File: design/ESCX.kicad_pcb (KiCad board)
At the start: 4 copper layers, 100 x 100 mm, 130 parts, among them J1 SWD, J10 Screw_Terminal_01x03, J11 Screw_Terminal_01x02, J2 Conn_Coaxial, J8 HALL_ENC, J9 USB_C_Receptacle_USB2.0_16P, Q1 IRF7854, Q2 IRF7854, Q3 IRF7854, Q4 IRF7854, Q5 IRF7854, Q6 IRF7854, SW1 SENSOR_VOLTAGE, U1 STM32F40X_LQFP64, U2 LM3671, U3 DRV8301, U4 nRF24L01P, U5 AD8418, U6 AD8418, U7 AD8418, X1 8MHz, X2 16MHz

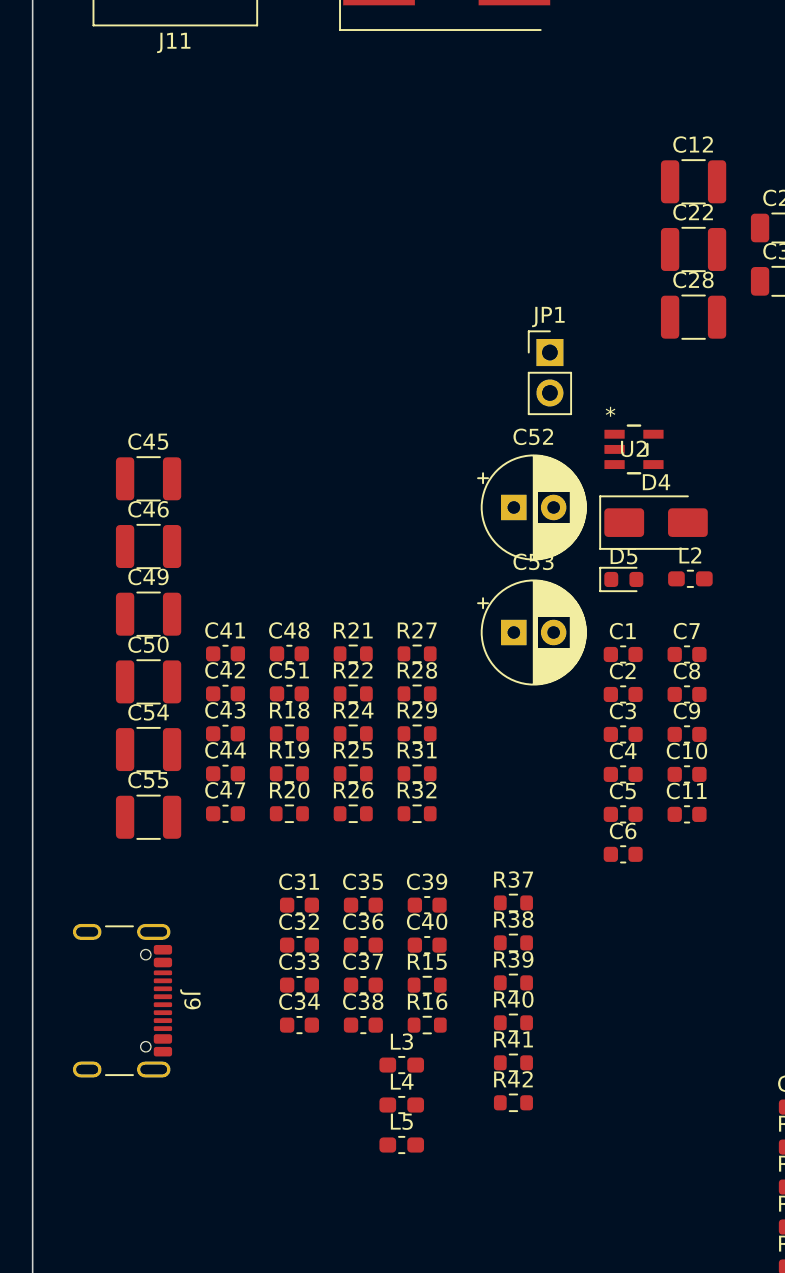
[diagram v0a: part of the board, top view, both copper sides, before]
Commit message: Ubico componentes de USB
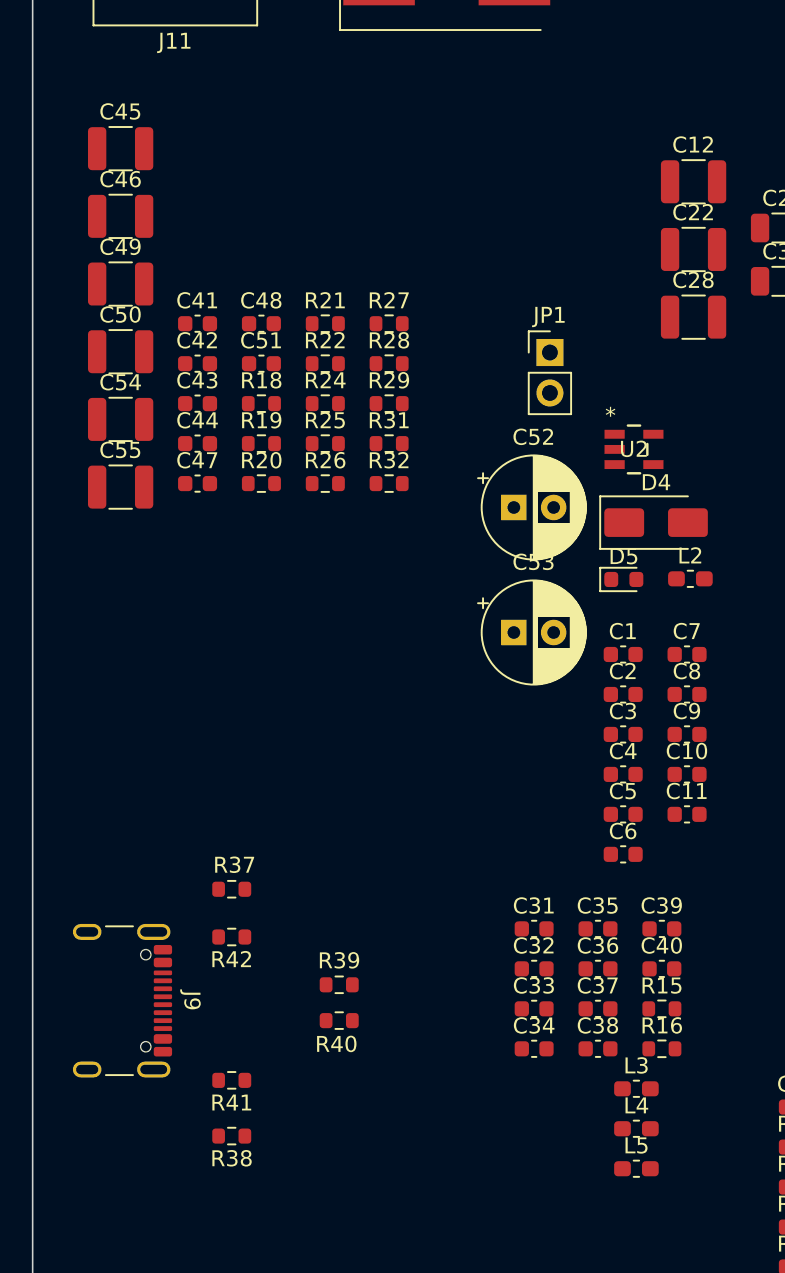
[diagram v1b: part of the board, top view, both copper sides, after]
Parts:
- moved R38 21.4 mm to (111.5, 115.5), turned to 180 degrees
- moved C41 20.8 mm to (109.4, 64.5)
- moved C42 20.8 mm to (109.4, 67.0)
- moved C44 20.8 mm to (109.4, 72.0)
- moved C45 20.8 mm to (104.5, 53.5)
- moved C46 20.8 mm to (104.5, 57.8)
- moved C47 20.8 mm to (109.4, 74.5)
- moved C48 20.8 mm to (113.4, 64.5)
- moved C49 20.8 mm to (104.5, 62.0)
- moved C50 20.8 mm to (104.5, 66.2)
- moved C51 20.8 mm to (113.4, 67.0)
- moved C54 20.8 mm to (104.5, 70.5)
- moved C55 20.8 mm to (104.5, 74.8)
- moved R19 20.8 mm to (113.4, 72.0)
- moved R20 20.8 mm to (113.4, 74.5)
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
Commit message: inicio ruteo de MCU y USB
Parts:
- moved X1 79.9 mm to (150.5, 119.2), turned to 180 degrees
- moved C33 30.2 mm to (109.8, 85.5)
- moved C37 30.2 mm to (113.8, 85.5)
- moved L4 30.2 mm to (116.2, 93.0)
- moved C31 30.2 mm to (109.8, 80.5)
- moved C32 30.2 mm to (109.8, 83.0)
- moved C34 30.2 mm to (109.8, 88.0)
- moved C35 30.2 mm to (113.8, 80.5)
- moved C36 30.2 mm to (113.8, 83.0)
- moved C38 30.2 mm to (113.8, 88.0)
- moved L3 30.2 mm to (116.2, 90.5)
- moved L5 30.2 mm to (116.2, 95.6)
- moved R15 30.2 mm to (117.8, 85.5)
- moved C39 30.2 mm to (117.8, 80.5)
- moved C40 30.2 mm to (117.8, 83.0)
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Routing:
- net /MCU/NRST: track 0.00 -> 25.1 mm, vias 0 -> 2
- net /MCU/SWCLK: track 0.00 -> 19.0 mm, vias 0 -> 2
- net Net-(J9-D+-PadA6): track 0.00 -> 18.3 mm
- net /MCU/USB_DM: track 0.00 -> 18.2 mm
- net Net-(U1-PH1-OSC_OUT): track 0.00 -> 17.1 mm
- net /MCU/USB_DP: track 0.00 -> 16.6 mm
- net /MCU/SWDIO: track 0.00 -> 16.3 mm
- net Net-(J9-VBUS-PadA4): track 0.00 -> 14.6 mm
- net Net-(J9-D--PadA7): track 0.00 -> 10.3 mm
- net Net-(U1-PH0-OSC_IN): track 0.00 -> 9.59 mm
- net Net-(J9-CC2): track 0.00 -> 9.51 mm
- net Net-(J9-CC1): track 0.00 -> 5.95 mm

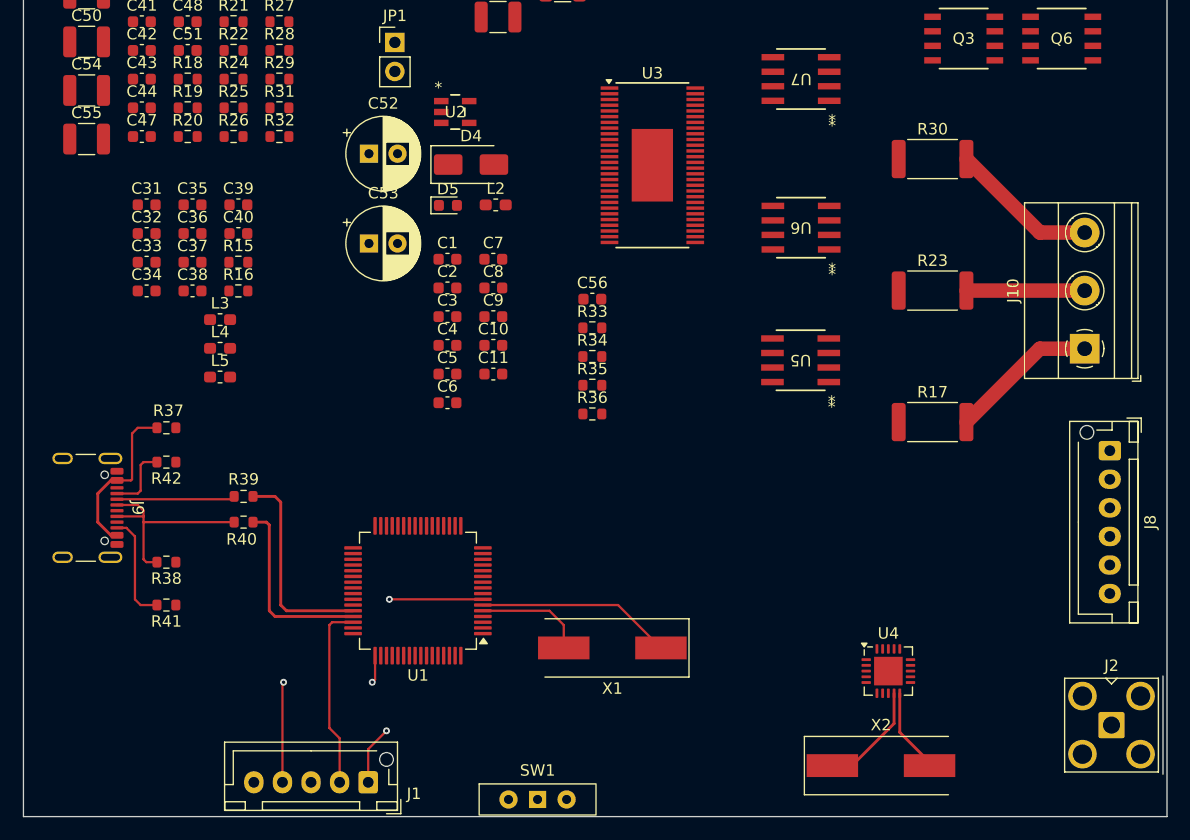
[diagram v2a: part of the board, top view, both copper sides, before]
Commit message: Continue rooteo del MCU y modulo BT
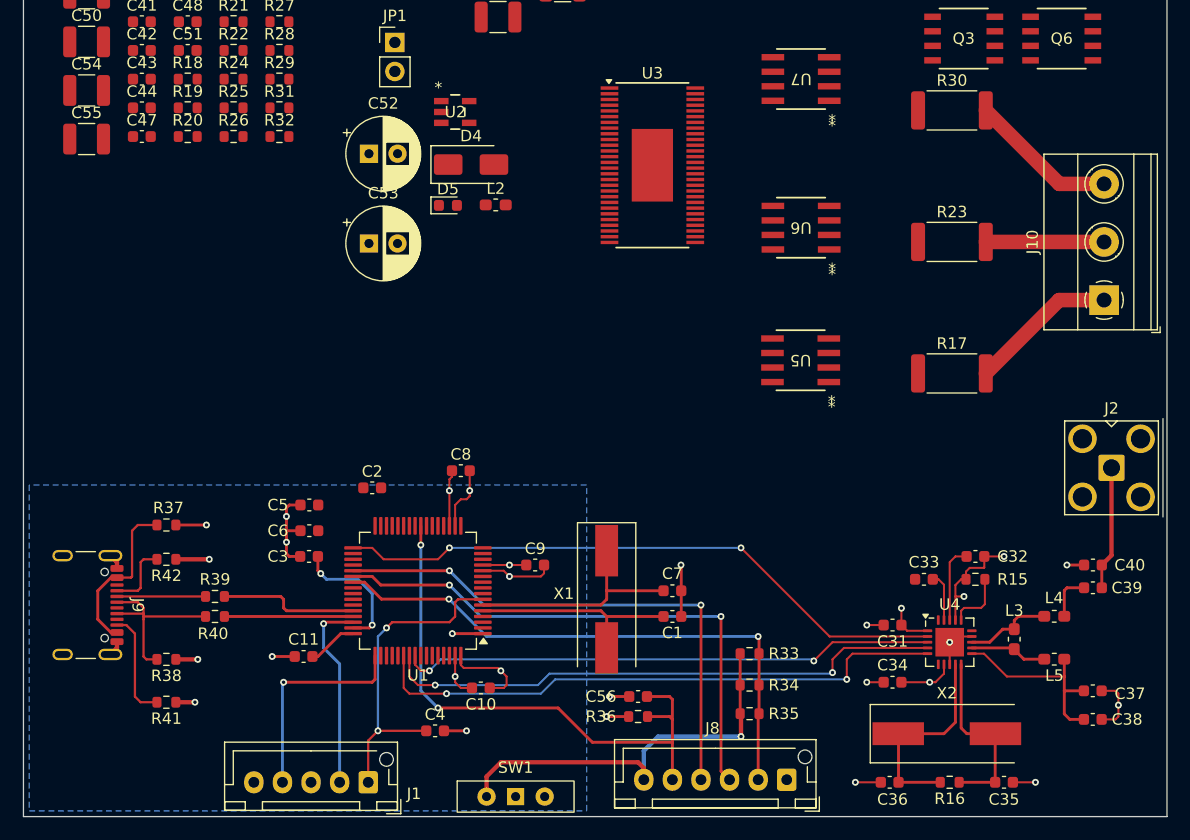
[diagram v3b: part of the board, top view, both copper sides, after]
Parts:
- moved C37 87.2 mm to (192.5, 123.0)
- moved C38 87.2 mm to (192.5, 125.5)
- moved C35 87.1 mm to (184.8, 131.0), turned to 180 degrees
- moved C39 81.9 mm to (192.5, 114.0), turned to 180 degrees
- moved C40 80.2 mm to (192.5, 112.0), turned to 180 degrees
- moved C32 77.8 mm to (182.2, 111.2)
- moved C36 77.6 mm to (174.8, 131.0)
- moved L5 77.0 mm to (189.1, 120.2), turned to 180 degrees
- moved L4 76.6 mm to (189.1, 116.5), turned to 180 degrees
- moved R16 75.6 mm to (180.0, 131.0), turned to 180 degrees
- moved C31 74.9 mm to (175.0, 117.2), turned to 180 degrees
- moved L3 74.9 mm to (185.6, 118.5), turned to -90 degrees
- moved C34 73.7 mm to (175.0, 122.2), turned to 180 degrees
- moved C33 73.4 mm to (177.8, 113.2)
- moved R15 70.2 mm to (182.2, 113.2)
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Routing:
- net GND1: track 0.00 -> 69.3 mm, vias 0 -> 20
- net /MCU/PB12: track 0.00 -> 54.3 mm, vias 0 -> 2
- net /MCU/PD2: track 0.00 -> 51.3 mm, vias 0 -> 2
- net /MCU/HALL_3: track 0.00 -> 50.0 mm, vias 0 -> 2
- net /MCU/TEMP_MOTOR: track 0.00 -> 49.9 mm, vias 0 -> 2
- net /MCU/PB3: track 0.00 -> 49.5 mm, vias 0 -> 2
- net /MCU/HALL_2: track 0.00 -> 48.2 mm, vias 0 -> 2
- net /MCU/PB4: track 0.00 -> 47.0 mm, vias 0 -> 2
- net /MCU/HALL_1: track 0.00 -> 46.9 mm, vias 0 -> 2
- net +3.3V: track 0.00 -> 42.8 mm, vias 0 -> 8
- net Net-(J8-Pin_6): track 0.00 -> 36.1 mm, vias 0 -> 1
- net Net-(U4-VDD_PA): track 0.00 -> 17.3 mm
- net Net-(U1-VCAP2): track 0.00 -> 11.4 mm, vias 0 -> 2
- net Net-(J2-In): track 0.00 -> 10.8 mm
- net Net-(U1-PH0-OSC_IN): track 9.59 -> 18.8 mm
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- added copper zone on In2.Cu, net +3.3V
- added copper zone on B.Cu, net +5V
- added copper zone on In1.Cu, net GND1

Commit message: Continuacion de Rooteo
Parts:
- moved C16 80.4 mm to (77.4, 73.0)
- moved C19 80.4 mm to (77.4, 80.6)
- moved R10 80.4 mm to (89.4, 73.0)
- moved R11 80.4 mm to (89.4, 75.5)
- moved R13 80.4 mm to (89.4, 80.6)
- moved C13 80.4 mm to (77.4, 70.5)
- moved C18 80.4 mm to (77.4, 78.0)
- moved C20 80.4 mm to (77.4, 83.1)
- moved C23 80.4 mm to (81.4, 70.5)
- moved C24 80.4 mm to (81.4, 73.0)
- moved C27 80.4 mm to (81.4, 80.6)
- moved C29 80.4 mm to (81.4, 83.1)
- moved R12 80.4 mm to (89.4, 78.0)
- moved R14 80.4 mm to (89.4, 83.1)
- moved R9 80.4 mm to (89.4, 70.5)
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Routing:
- net +5V: track 2.67 -> 27.8 mm, vias 1 -> 2
- net /DRV8301/FAULT: track 0.00 -> 24.8 mm, vias 0 -> 2
- net /DRV8301/EN_GATE: track 0.00 -> 22.9 mm, vias 0 -> 2
- net /DRV8301/SDI: track 0.00 -> 21.5 mm, vias 0 -> 2
- net /DRV8301/SDO: track 0.00 -> 19.2 mm, vias 0 -> 2
- net /DRV8301/SCLK: track 0.00 -> 17.7 mm, vias 0 -> 2
- net GND1: track 69.3 -> 79.8 mm, vias 20 -> 25
- net Net-(U3-SS_TR): track 0.00 -> 10.2 mm
- net Net-(D4-K): track 0.00 -> 9.41 mm
- net SUPPLY: track 0.00 -> 7.69 mm
- net Net-(U3-BST_BK): track 0.00 -> 7.00 mm
- net +3.3V: track 42.8 -> 48.4 mm, vias 8 -> 11
- net /MCU/PB12: track 54.3 -> 58.1 mm
- net Net-(U1-VCAP1): track 0.00 -> 3.34 mm

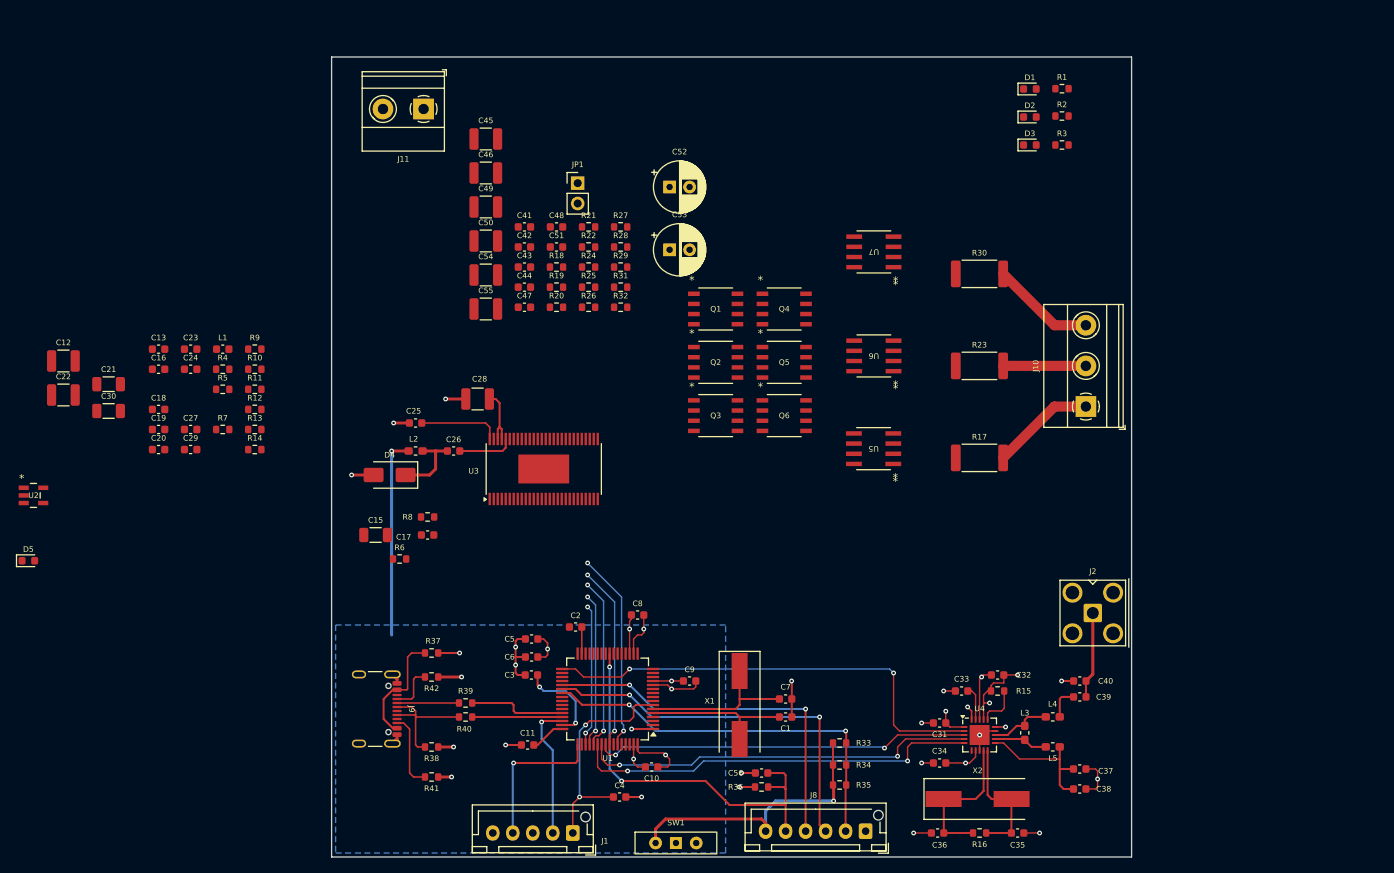
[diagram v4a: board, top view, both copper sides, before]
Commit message: Ruteo del driver y ubicacion de MOSFETs
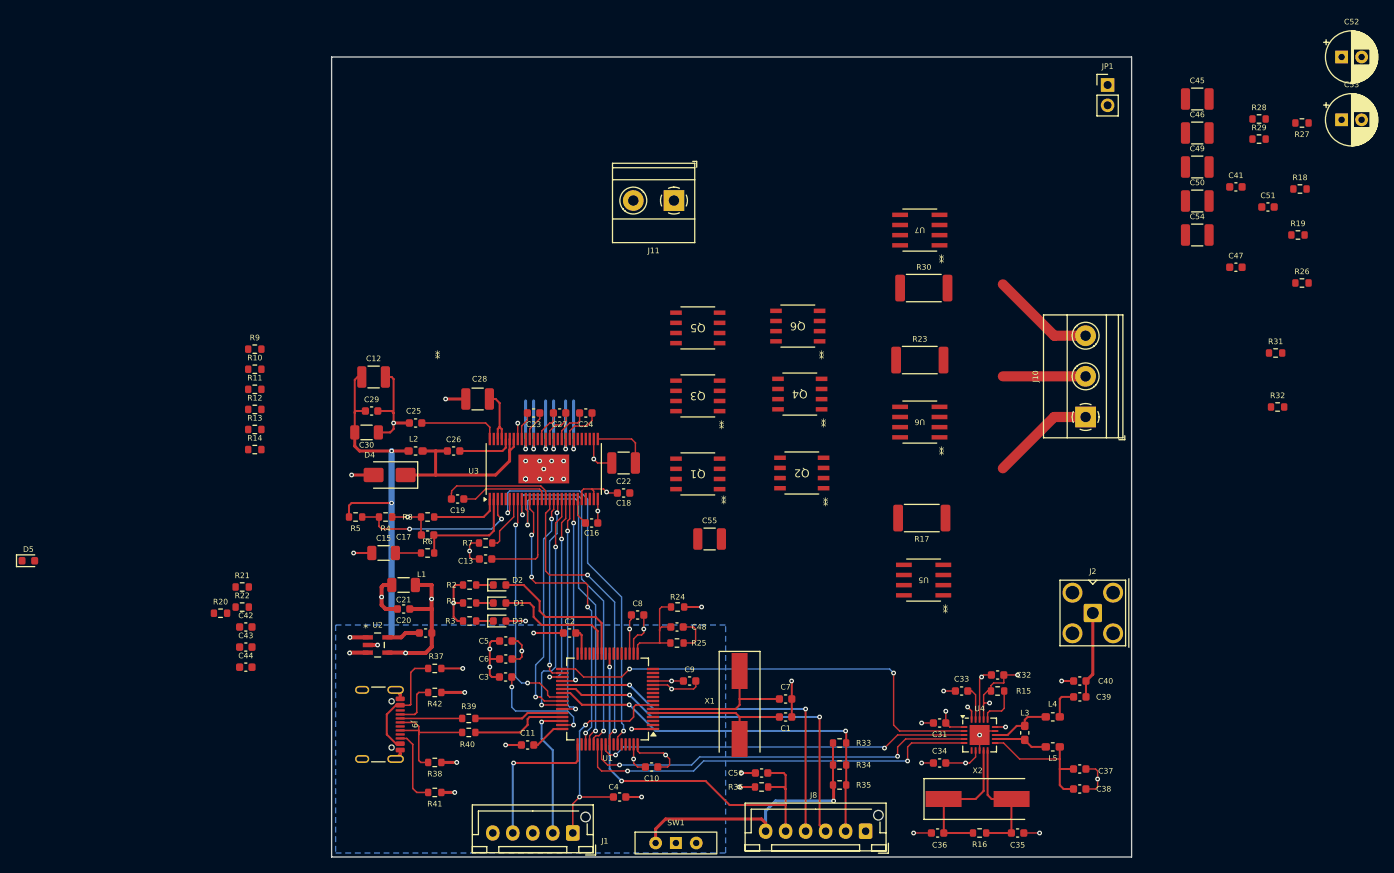
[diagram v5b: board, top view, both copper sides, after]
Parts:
- Q1, Q2, Q3, Q4, Q5, Q6: footprint crf1:SO-8_INF -> crf1:SO-8_INF_IRF7854
- moved R1 98.1 mm to (116.2, 102.2), turned to 180 degrees
- moved R3 95.0 mm to (116.2, 104.5)
- moved R2 94.4 mm to (116.2, 100.0), turned to 180 degrees
- moved R18 93.4 mm to (220.0, 50.5)
- moved R19 92.9 mm to (219.8, 56.2)
- moved D1 92.3 mm to (120.0, 102.2)
- moved R26 89.2 mm to (220.3, 62.2)
- moved D3 89.1 mm to (120.0, 104.5)
- moved C51 89.1 mm to (216.0, 52.8)
- moved C45 89.1 mm to (207.2, 39.2)
- moved C46 89.1 mm to (207.2, 43.5)
- moved C49 89.1 mm to (207.2, 47.8)
- moved C50 89.1 mm to (207.2, 52.0)
- moved C54 89.1 mm to (207.2, 56.2)
- moved C41 89.1 mm to (212.0, 50.2)
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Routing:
- net GND1: track 79.8 -> 141.2 mm, vias 25 -> 44
- net /DRV8301/INH_B: track 0.00 -> 30.0 mm, vias 0 -> 2
- net /DRV8301/CS: track 0.00 -> 29.5 mm, vias 0 -> 2
- net /DRV8301/INH_A: track 0.00 -> 29.2 mm, vias 0 -> 2
- net /DRV8301/INH_C: track 0.08 -> 28.8 mm, vias 0 -> 2
- net +5V: track 27.8 -> 55.0 mm, vias 2 -> 5
- net /DRV8301/SDO: track 19.2 -> 44.6 mm
- net /DRV8301/INL_B: track 0.00 -> 25.2 mm, vias 0 -> 2
- net +3.3V: track 48.4 -> 73.4 mm, vias 11 -> 16
- net /DRV8301/INL_C: track 0.00 -> 24.7 mm, vias 0 -> 2
- net /DRV8301/INL_A: track 0.00 -> 23.6 mm, vias 0 -> 2
- net /DRV8301/SDI: track 21.5 -> 44.7 mm
- net /DRV8301/FAULT: track 24.8 -> 47.7 mm
- net Net-(U3-VSENSE): track 0.00 -> 22.0 mm, vias 0 -> 2
- net /DRV8301/SCLK: track 17.7 -> 38.1 mm, vias 2 -> 4
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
